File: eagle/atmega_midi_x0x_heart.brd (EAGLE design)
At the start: 100 x 80 mm, 33 parts, among them J11_VCF_CUTOFF 22-23-2021, U1 ATMEGA328P_PDIP, U2 TLV2372IP

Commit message: digital pot and midi out
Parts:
- added MIDI_OUT_THRU, RES1, RES2, RES_POT: (no value), con-lstb:MA03-1
- added R9: 220, rcl:0207/10
- added U$1: MCP42050-E/P, MCP42050-E_P:DIP254P762X432-14
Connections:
- new net N$31: RES1.2, U$1.9
- new net N$32: RES1.1, U$1.8
- new net N$33: RES1.3, U$1.10
- new net N$34: RES2.2, U$1.6
- new net N$35: RES2.1, U$1.7
- new net N$36: RES2.3, U$1.5
- new net N$37: U$1.3, U1.14
- new net N$38: RES_POT.2, U1.27
- new net N$39: MIDI_OUT_THRU.1, R9.2
- new net N$40: U$1.1, U1.4
- new net N$41: U$1.2, U1.13
- new net N$42: MIDI_OUT_THRU.2, U1.3
- net +5V: now also R9.1, RES_POT.1, U$1.11, U$1.12, U$1.14, U1.21
- net GND: now also MIDI_OUT_THRU.3, RES_POT.3, U$1.4
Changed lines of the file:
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@@
 <attribute name="OC_FARNELL" value="8455031" x="29.464" y="22.86" size="1.778" layer="27" rot="R90" display="off"/>
+</element>
+<element name="U$1" library="MCP42050-E_P" package="DIP254P762X432-14" value="MCP42050-E/P" x="-3.81" y="6.35"/>
+<element name="RES1" library="con-lstb" package="MA03-1" value="" x="-7.62" y="-3.81">
+<attribute name="OC_NEWARK" value="unknown" x="-7.62" y="-3.81" size="1.778" layer="27" display="off"/>
+<attribute name="MPN" value="" x="-7.62" y="-3.81" size="1.778" layer="27" display="off"/>
+<attribute name="MF" value="" x="-7.62" y="-3.81" size="1.778" layer="27" display="off"/>
+<attribute name="OC_FARNELL" value="unknown" x="-7.62" y="-3.81" size="1.778" layer="27" display="off"/>
+</element>
+<element name="RES2" library="con-lstb" package="MA03-1" value="" x="-7.62" y="-10.16">
+<attribute name="OC_NEWARK" value="unknown" x="-7.62" y="-10.16" size="1.778" layer="27" display="off"/>
+<attribute name="MPN" value="" x="-7.62" y="-10.16" size="1.778" layer="27" display="off"/>
+<attribute name="MF" value="" x="-7.62" y="-10.16" size="1.778" layer="27" display="off"/>
+<attribute name="OC_FARNELL" value="unknown" x="-7.62" y="-10.16" size="1.778" layer="27" display="off"/>
+</element>
+<element name="RES_POT" library="con-lstb" package="MA03-1" value="" x="-7.62" y="-16.51">
+<attribute name="OC_NEWARK" value="unknown" x="-7.62" y="-16.51" size="1.778" layer="27" display="off"/>
+<attribute name="MPN" value="" x="-7.62" y="-16.51" size="1.778" layer="27" display="off"/>
+<attribute name="MF" value="" x="-7.62" y="-16.51" size="1.778" layer="27" display="off"/>
+<attribute name="OC_FARNELL" value="unknown" x="-7.62" y="-16.51" size="1.778" layer="27" display="off"/>
+</element>
+<element name="R9" library="rcl" package="0207/10" value="220" x="-7.62" y="-22.86"/>
+<element name="MIDI_OUT_THRU" library="con-lstb" package="MA03-1" value="" x="-7.62" y="-27.94">
+<attribute name="OC_NEWARK" value="unknown" x="-7.62" y="-27.94" size="1.778" layer="27" display="off"/>
+<attribute name="MPN" value="" x="-7.62" y="-27.94" size="1.778" layer="27" display="off"/>
+<attribute name="MF" value="" x="-7.62" y="-27.94" size="1.778" layer="27" display="off"/>
+<attribute name="OC_FARNELL" value="unknown" x="-7.62" y="-27.94" size="1.778" layer="27" display="off"/>
 </element>
 </elements>
@@
 <via x="47.117" y="6.731" extent="1-16" drill="0.8" shape="square"/>
 <wire x1="47.117" y1="6.731" x2="46.482" y2="4.826" width="0.8128" layer="16"/>
+<contactref element="U$1" pad="14"/>
+<contactref element="U$1" pad="11"/>
+<contactref element="U$1" pad="12"/>
+<contactref element="RES_POT" pad="1"/>
+<contactref element="U1" pad="21"/>
+<contactref element="R9" pad="1"/>
+<wire x1="51.562" y1="23.876" x2="49.022" y2="27.686" width="0" layer="19" extent="16-16"/>
+<wire x1="-3.81" y1="21.59" x2="26.162" y2="40.386" width="0" layer="19" extent="16-16"/>
+<wire x1="-3.81" y1="16.51" x2="-3.81" y2="21.59" width="0" layer="19" extent="1-1"/>
+<wire x1="-3.81" y1="13.97" x2="-3.81" y2="16.51" width="0" layer="19" extent="1-1"/>
+<wire x1="-10.16" y1="-16.51" x2="-3.81" y2="13.97" width="0" layer="19" extent="1-1"/>
+<wire x1="-12.7" y1="-22.86" x2="-10.16" y2="-16.51" width="0" layer="19" extent="1-1"/>
 </signal>
 <signal name="+12V">
@@
 <wire x1="23.622" y1="35.306" x2="22.352" y2="35.306" width="0.8128" layer="16"/>
 <wire x1="22.352" y1="35.306" x2="21.082" y2="36.576" width="0.8128" layer="16"/>
+<contactref element="U$1" pad="4"/>
+<contactref element="RES_POT" pad="3"/>
+<contactref element="MIDI_OUT_THRU" pad="3"/>
+<wire x1="-11.43" y1="13.97" x2="17.272" y2="26.416" width="0" layer="19" extent="16-16"/>
+<wire x1="-5.08" y1="-16.51" x2="-11.43" y2="13.97" width="0" layer="19" extent="1-1"/>
+<wire x1="-5.08" y1="-27.94" x2="-5.08" y2="-16.51" width="0" layer="19" extent="1-1"/>
 </signal>
 <signal name="N$24">
@@
 <wire x1="14.732" y1="27.686" x2="14.732" y2="32.766" width="0.8128" layer="16"/>
 </signal>
+<signal name="N$31">
+<contactref element="U$1" pad="9"/>
+<contactref element="RES1" pad="2"/>
+<wire x1="-3.81" y1="8.89" x2="-7.62" y2="-3.81" width="0" layer="19" extent="1-1"/>
+</signal>
+<signal name="N$32">
+<contactref element="U$1" pad="8"/>
+<contactref element="RES1" pad="1"/>
+<wire x1="-3.81" y1="6.35" x2="-10.16" y2="-3.81" width="0" layer="19" extent="1-1"/>
+</signal>
+<signal name="N$33">
+<contactref element="U$1" pad="10"/>
+<contactref element="RES1" pad="3"/>
+<wire x1="-5.08" y1="-3.81" x2="-3.81" y2="11.43" width="0" layer="19" extent="1-1"/>
+</signal>
+<signal name="N$34">
+<contactref element="U$1" pad="6"/>
+<contactref element="RES2" pad="2"/>
+<wire x1="-11.43" y1="8.89" x2="-7.62" y2="-10.16" width="0" layer="19" extent="1-1"/>
+</signal>
+<signal name="N$35">
+<contactref element="U$1" pad="7"/>
+<contactref element="RES2" pad="1"/>
+<wire x1="-11.43" y1="6.35" x2="-10.16" y2="-10.16" width="0" layer="19" extent="1-1"/>
+</signal>
+<signal name="N$36">
+<contactref element="U$1" pad="5"/>
+<contactref element="RES2" pad="3"/>
+<wire x1="-11.43" y1="11.43" x2="-5.08" y2="-10.16" width="0" layer="19" extent="1-1"/>
+</signal>
+<signal name="N$40">
+<contactref element="U$1" pad="1"/>
+<contactref element="U1" pad="4"/>
+<wire x1="-11.43" y1="21.59" x2="56.642" y2="17.526" width="0" layer="19" extent="1-1"/>
+</signal>
+<signal name="N$41">
+<contactref element="U$1" pad="2"/>
+<contactref element="U1" pad="13"/>
+<wire x1="-11.43" y1="19.05" x2="56.642" y2="40.386" width="0" layer="19" extent="1-1"/>
+</signal>
+<signal name="N$37">
+<contactref element="U$1" pad="3"/>
+<contactref element="U1" pad="14"/>
+<wire x1="-11.43" y1="16.51" x2="56.642" y2="42.926" width="0" layer="19" extent="1-1"/>
+</signal>
+<signal name="N$38">
+<contactref element="RES_POT" pad="2"/>
+<contactref element="U1" pad="27"/>
+<wire x1="-7.62" y1="-16.51" x2="49.022" y2="12.446" width="0" layer="19" extent="1-1"/>
+</signal>
+<signal name="N$39">
+<contactref element="MIDI_OUT_THRU" pad="1"/>
+<contactref element="R9" pad="2"/>
+<wire x1="-2.54" y1="-22.86" x2="-10.16" y2="-27.94" width="0" layer="19" extent="1-1"/>
+</signal>
+<signal name="N$42">
+<contactref element="U1" pad="3"/>
+<contactref element="MIDI_OUT_THRU" pad="2"/>
+<wire x1="-7.62" y1="-27.94" x2="56.642" y2="14.986" width="0" layer="19" extent="1-1"/>
+</signal>
 </signals>

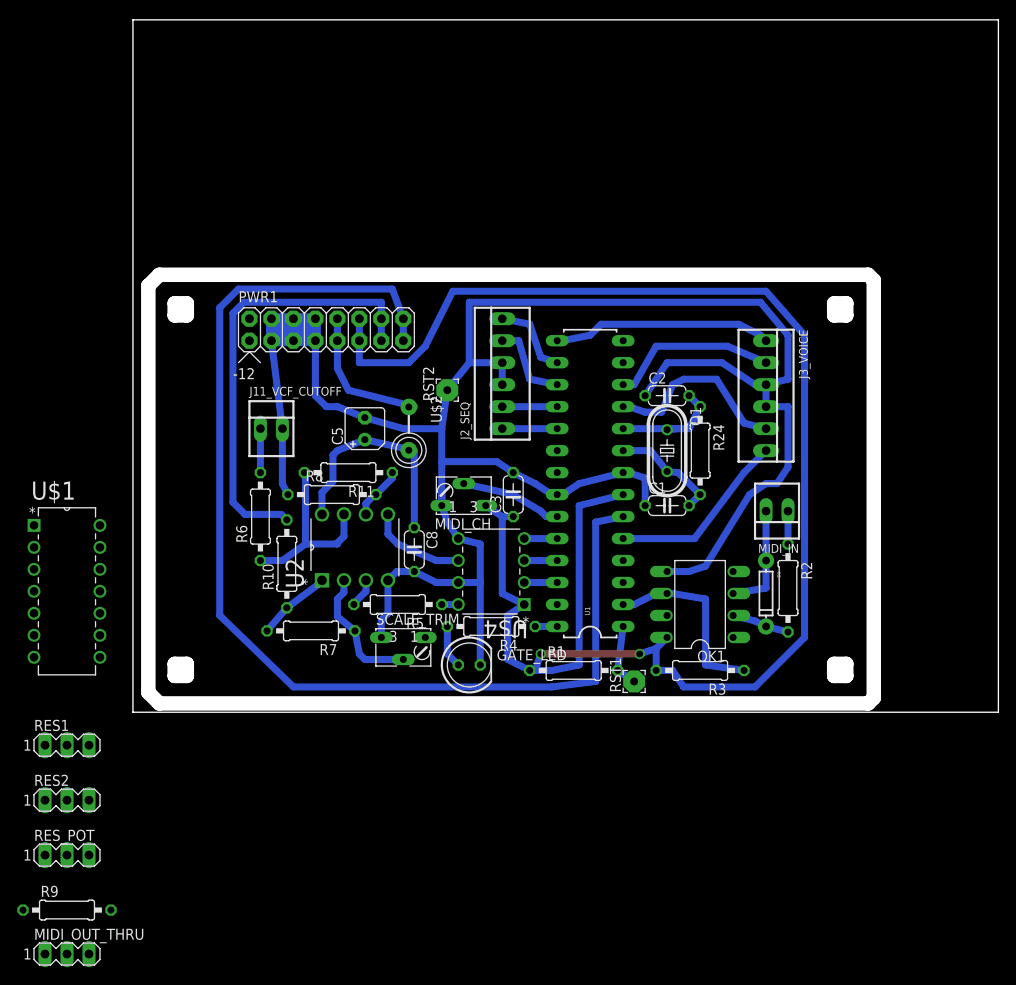
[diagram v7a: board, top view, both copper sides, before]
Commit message: initial layout for res control version
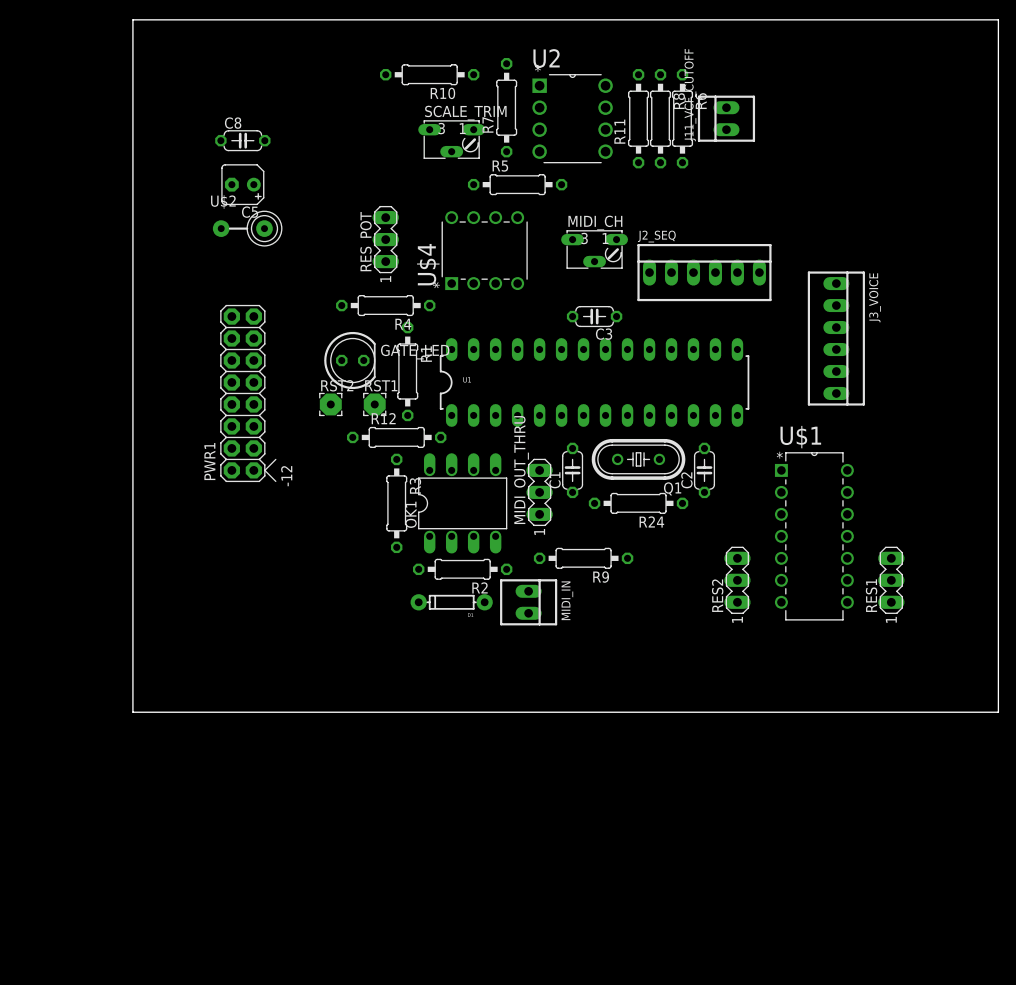
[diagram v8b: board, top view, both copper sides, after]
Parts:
- added R12: 2k4, rcl:0207/10
- C3: value .1uF -> 100n
- moved RES1 97.1 mm to (87.6, 15.2), turned to 90 degrees
- moved U$1 86.6 mm to (82.5, 12.7)
- moved RES2 81.5 mm to (69.8, 15.2), turned to 90 degrees
- moved RES_POT 80.1 mm to (29.2, 54.6), turned to 90 degrees
- moved MIDI_OUT_THRU 76.3 mm to (47.0, 25.4), turned to 90 degrees
- moved R9 72.2 mm to (52.1, 17.8), turned to 180 degrees
- moved R6 67.0 mm to (63.5, 68.6), turned to 270 degrees
- moved R7 64.5 mm to (43.2, 69.8), turned to 90 degrees
- moved J11_VCF_CUTOFF 63.6 mm to (68.6, 68.6), turned to 90 degrees
- moved SCALE_TRIM 58.9 mm to (36.8, 67.3)
- moved R10 58.9 mm to (34.3, 73.7), turned to 180 degrees
- moved R8 57.7 mm to (61.0, 68.6), turned to 270 degrees
- moved R11 52.9 mm to (58.4, 68.6), turned to 90 degrees
- moved C8 51.2 mm to (12.7, 66.0), turned to 0 degrees
- moved R5 50.5 mm to (44.5, 61.0), turned to 0 degrees
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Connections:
- new net N$44: OK1.7, R12.2
- net GND: now also R12.1
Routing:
- net GND: track 248.1 -> 0.00 mm
- net +5V: track 193.7 -> 0.00 mm, vias 2 -> 0
- net N$22: track 131.1 -> 0.00 mm
- net N$15: track 51.0 -> 0.00 mm
- net +12V: track 26.9 -> 0.00 mm
- net N$9: track 25.3 -> 0.00 mm
- net N$30: track 22.0 -> 0.00 mm
- net N$16: track 21.8 -> 0.00 mm
- net N$17: track 21.5 -> 0.00 mm
- net N$1: track 21.4 -> 0.00 mm
- net N$10: track 19.5 -> 0.00 mm
- net N$11: track 17.0 -> 0.00 mm
- net N$12: track 15.2 -> 0.00 mm
- net N$5: track 13.5 -> 0.00 mm
- net N$4: track 12.9 -> 0.00 mm
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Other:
- outline, holes or cut-outs redrawn
